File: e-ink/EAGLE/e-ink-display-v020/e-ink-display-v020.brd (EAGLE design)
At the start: 100 x 90 mm, 170 parts, among them J01M USBUSB-MICROB-PAD-EXTEND, J01S MICROSD, J02S EINKED060SC4, Q01B IRLML6402PbF, Q02B IRLML6402PbF, Q02M MMDT3904, Q2 IRLML6402PbF (DNP), SW01M SWITCHSIDE-SLIDE, U01B BQ24075, U01M STM32F10XRXT6, U01S ADXL345, U02B R8008-33, U03B LT1945-IMS#PBF, U04B LM79L15, U05B LM78L15, U06B LM358-DGKR, U1 MCP73831, Y01M 32kHz, Y02M 8MHz

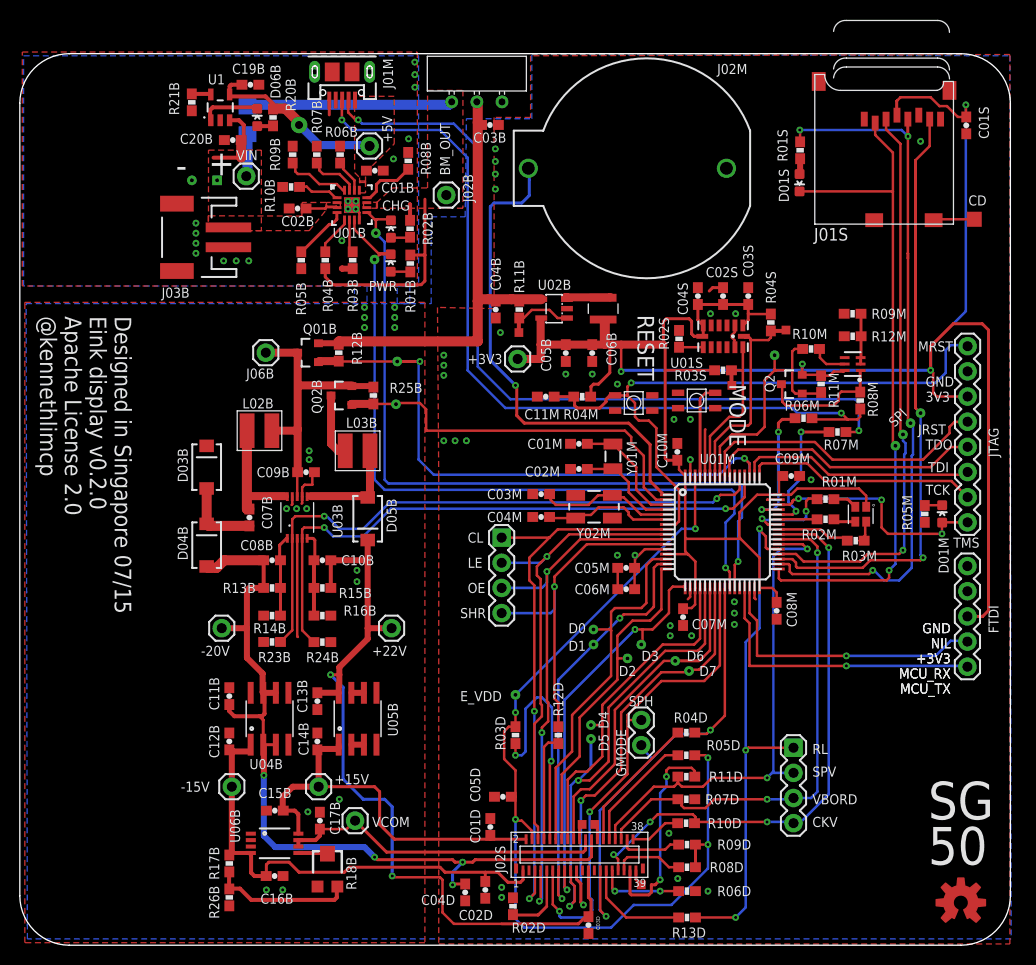
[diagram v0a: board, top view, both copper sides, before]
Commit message: Polishing e-ink-display-v020 to fit my personal taste
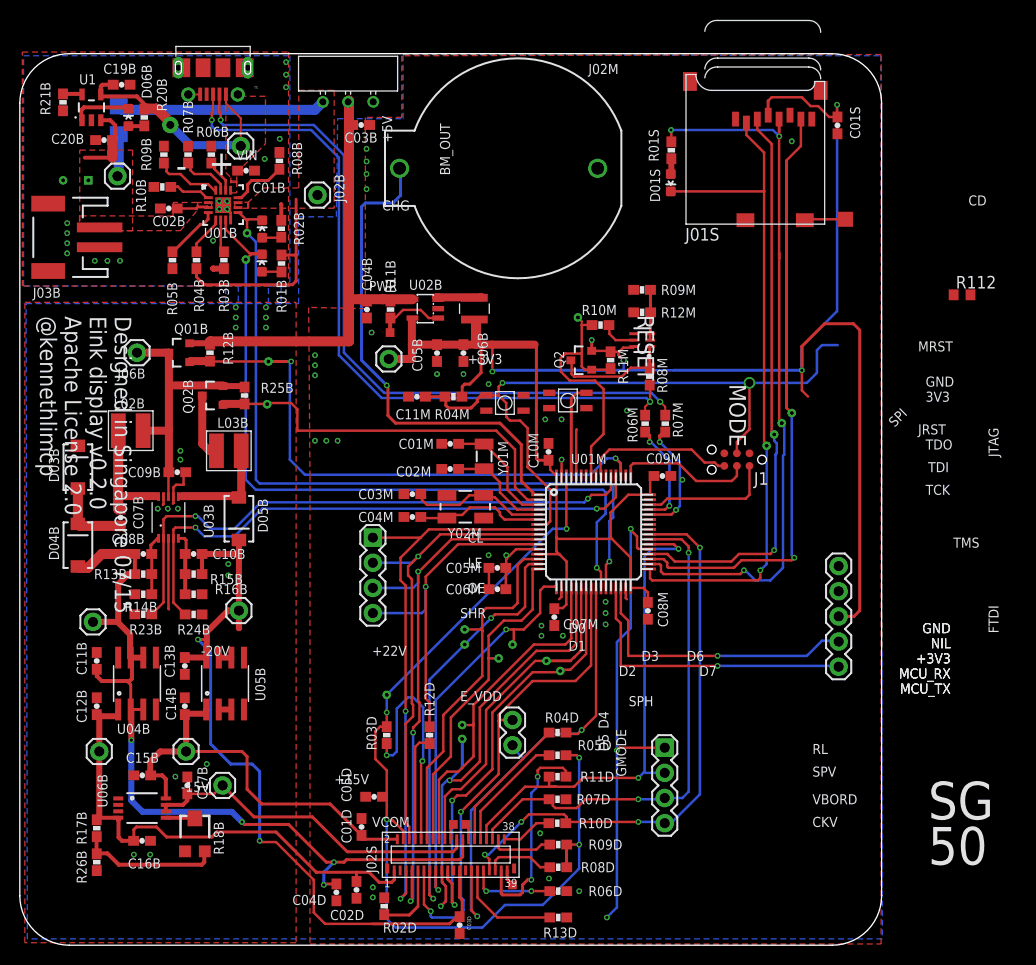
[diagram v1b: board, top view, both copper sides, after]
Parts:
- removed C02S: 10uF, 6.3V, X5R, kennethlimcp:0603-CAP
- removed C03S, C04S: 0.1uF, 6.3V, X5R, kennethlimcp:0603-CAP
- removed D01M: BLUE, SparkFun-LED:LED-0603
- removed D02M: RGB-LED-CLMVB-FKARGB, Spark:PLCC4-2MM-RGB
- removed J01M: USBUSB-MICROB-PAD-EXTEND, Spark:USB-MICROB-SLOT-HOLE-EXTEND
- removed JP1: (no value), SparkFun-Connectors:1X08_ROUND
- removed LOGO1: OSHW-LOGOPAD, kennethlimcp:OSHW-LOGO-M-PAD
- removed R01M, R02M, R03M, R05M: 1K, 1%, kennethlimcp:0603-RES
- removed R02S: 0 Ohm, kennethlimcp:0603-RES
- removed R03S, R04S: 4.7K, 1%, kennethlimcp:0603-RES
- removed TP17M, TP18M: TP1, Spark:TP35_BOT
- removed U01S: ADXL345, SparkFun-Sensors:LGA14
- added J1: (no value), tag-connect:TC2030-MCP-NL
- added J2: 105017-0001, 105017-0001:MOLEX_105017-0001
- added R112: 10K, rcl:R0603
- moved Q02M 21.4 mm to (62.8, 61.1)
- moved Q2 21.4 mm to (56.7, 59.0)
- moved R08M 21.4 mm to (63.6, 57.4)
- moved R09M 21.4 mm to (62.8, 66.2)
- moved R10M 21.4 mm to (58.6, 62.6)
- moved R11M 21.4 mm to (59.6, 59.1)
- moved R12M 21.4 mm to (62.8, 63.9)
- moved TP06M 20.2 mm to (56.3, 63.4)
- moved R07M 17.4 mm to (65.2, 52.7), turned to 90 degrees
- moved R06M 16.0 mm to (63.1, 52.7), turned to 90 degrees
- moved J08B 15.5 mm to (22.1, 33.8)
- moved C11B 13.8 mm to (7.77, 28.7)
- moved C12B 13.8 mm to (7.77, 24.1)
- moved C13B 13.8 mm to (16.7, 28.2)
- moved C14B 13.8 mm to (16.7, 24.1)
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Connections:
- net MCU_USBM renamed MCU_USB_N
- net MCU_USBP renamed MCU_USB_P
- removed net !MCU_RST: C11M.1, JP1.1, R04M.1, S02M.1, U01M.7
- removed net JNTRST: JP1.4, U01M.56
- removed net JTAG_TRST: R02S.1
- removed net JTCK: JP1.7, U01M.49
- removed net JTDI: JP1.6, U01M.50
- removed net JTDO: JP1.5, U01M.55
- removed net JTMS: D01M.A, JP1.8, U01M.46
- removed net MCU_SCL: R04S.1, TP18M.P$1, U01M.58, U01S.14
- removed net MCU_SDA: R03S.1, TP17M.P$1, U01M.59, U01S.13
- removed net N$: J01M.D+, R06M.2, R08M.1
- removed net N$10: R02S.2, U01S.8
- removed net N$100: J01M.D-, R07M.2
- removed net N$14: D02M.RED, R01M.2
- removed net N$21: R11B.1, TP01B.P$1, U02B.1
- removed net N$38: D01M.C, R05M.1
- removed net R02M: D02M.GREEN, R02M.2
- removed net R03M: D02M.BLUE, R03M.2
- removed net RGB_BLUE: R03M.1, U01M.41
- removed net RGB_GREEN: R02M.1, U01M.43
- removed net RGB_RED: R01M.1, U01M.42
- removed net VBUS: C01B.2, C19B.2, J01B.1, J01M.VBUS, R20B.1, U01B.13, U1.4
- new net !RST: C11M.1, J1.3, R04M.1, R112.2, S02M.1, U01M.7
- new net MCU_USB_R_N: J2.2, R07M.2
- new net MCU_USB__R_P: J2.3, R06M.2, R08M.1
- new net N$20: U06B.1, U06B.2
- new net SWD_CLK: J1.4, U01M.49
- new net SWD_IO: J1.2, U01M.46
- new net SWO: J1.6, U01M.55
- net +3V3: now also J1.1, R112.1; no longer C02S.1, C03S.1, C04S.1, D02M.CA, JP1.3, R03S.2, R04S.2, U01S.1, U01S.6, U01S.7
- net EINK_RL: no longer R13D.1
- net GND: now also J1.5, J2.5, J2.MH1, J2.MH2, J2.MH3, J2.MH4, J2.P$10, J2.P$11, J2.P$8, J2.P$9, R11B.1, TP01B.P$1, U02B.1; no longer C02S.2, C03S.2, C04S.2, J01M.GND, JP1.2, R05M.2, U01S.12, U01S.2, U01S.4, U01S.5
- net N$6: now also U06B.3
- net VUSB: now also C01B.2, C19B.2, J01B.1, J2.1, R20B.1, U01B.13, U1.4
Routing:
- net N$: track 84.2 -> 0.00 mm, vias 2 -> 0
- net N$100: track 82.2 -> 0.00 mm, vias 2 -> 0
- net MCU_USB__R_P: track 0.00 -> 74.0 mm, vias 0 -> 2
- net MCU_USB_R_N: track 0.00 -> 72.2 mm, vias 0 -> 2
- net !RST: track 0.00 -> 71.9 mm, vias 0 -> 2
- net !MCU_RST: track 64.4 -> 0.00 mm, vias 1 -> 0
- net +3V3: track 248.0 -> 209.8 mm, vias 4 -> 5
- net JNTRST: track 30.0 -> 0.00 mm
- net JTDO: track 27.7 -> 0.00 mm
- net VUSB: track 0.00 -> 24.9 mm, vias 0 -> 1
- net JTDI: track 23.9 -> 0.00 mm
- net JTMS: track 23.6 -> 0.00 mm, vias 3 -> 0
- net JTCK: track 23.5 -> 0.00 mm
- net MCU_SCL: track 21.5 -> 0.00 mm
- net VBUS: track 19.1 -> 0.00 mm, vias 1 -> 0
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- added copper zone on layer 1, net VUSB
- removed copper zone on layer 1, net VBUS
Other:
- board size 100 x 90 mm -> 87 x 90 mm
